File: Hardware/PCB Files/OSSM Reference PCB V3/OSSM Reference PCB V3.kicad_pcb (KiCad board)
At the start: 4 copper layers, 30 x 100 mm, 64 parts, among them J1 Screw_Terminal_01x02, J2 Screw_Terminal_01x02, J3 RJ45, J4 Conn_01x04, J5 USB_C_Receptacle_USB2.0_16P, J6 Conn_01x04, J7 Conn_01x03, Q1 BC817, Q2 BC817, Q4 40P04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

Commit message: Improved documentation and silkscreen
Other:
- board text added: "5V"
- board text added: "A"
- board text added: "B"
- board text added: "DIR"
- board text added: "GND"
- board text added: "IF YOU CAN READ THIS, YOU'VE VOIDED THE WARRANTY"
- board text added: "MTR+"
- board text added: "OSSM v3.0 Beta 1 2024/08/21"
- board text added: "PUL"
- board text added: "VDD"
- board text added: "VOID MY WARRANTY BABY! THIS IS OPEN SOURCE!!!"

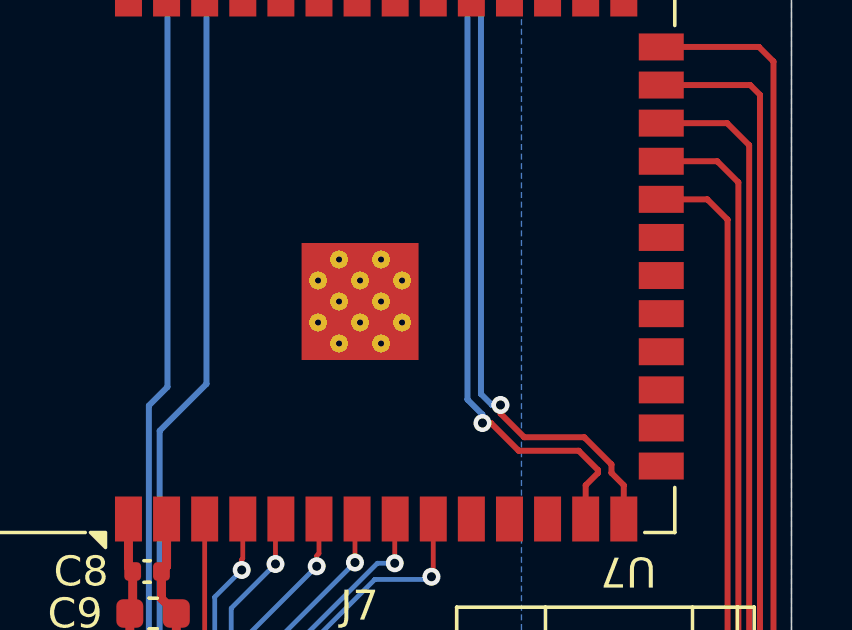
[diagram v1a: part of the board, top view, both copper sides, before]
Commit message: Last double check before ordering
Add Test points and Resistor Part numbers
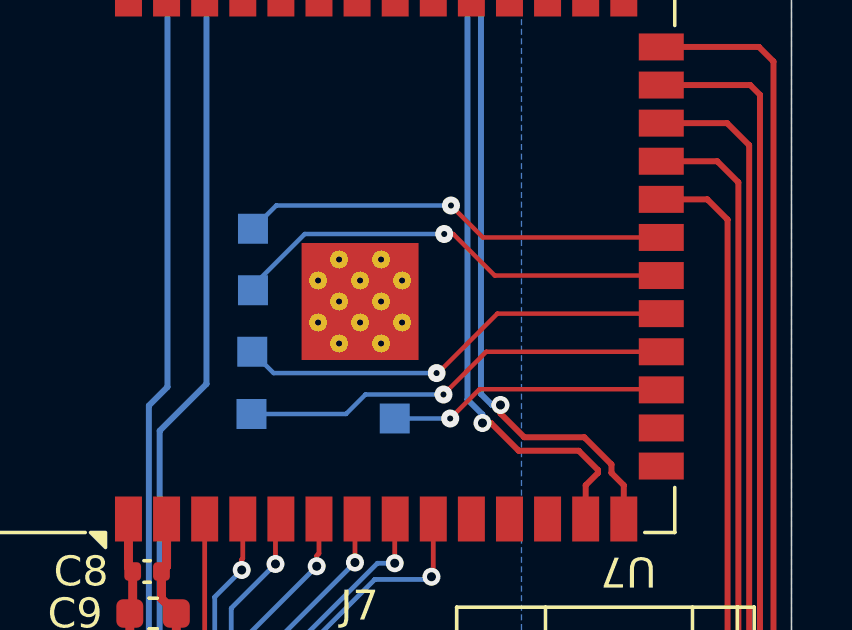
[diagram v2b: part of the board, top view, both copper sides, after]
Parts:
- added TP1: TestPoint, TestPoint:TestPoint_Pad_1.0x1.0mm, B.Cu at (81.8, 89.2)
- added TP2: TestPoint, TestPoint:TestPoint_Pad_1.0x1.0mm, B.Cu at (77.0, 89.0)
- added TP3: TestPoint, TestPoint:TestPoint_Pad_1.0x1.0mm, B.Cu at (77.0, 86.9)
- added TP4: TestPoint, TestPoint:TestPoint_Pad_1.0x1.0mm, B.Cu at (77.0, 84.9)
- added TP5: TestPoint, TestPoint:TestPoint_Pad_1.0x1.0mm, B.Cu at (77.0, 82.8)
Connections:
- U7 pad 17: unconnected-(U7-IO9-Pad17) -> Net-(U7-IO9)
- U7 pad 18: unconnected-(U7-IO10-Pad18) -> Net-(U7-IO10)
- U7 pad 19: unconnected-(U7-IO11-Pad19) -> Net-(U7-IO11)
- U7 pad 20: unconnected-(U7-IO12-Pad20) -> Net-(U7-IO12)
- U7 pad 21: unconnected-(U7-IO13-Pad21) -> Net-(U7-IO13)
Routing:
- net Net-(U7-IO12): track 0.00 -> 15.0 mm, vias 0 -> 1
- net Net-(U7-IO11): track 0.00 -> 14.8 mm, vias 0 -> 1
- net Net-(U7-IO10): track 0.00 -> 14.5 mm, vias 0 -> 1
- net Net-(U7-IO13): track 0.00 -> 14.4 mm, vias 0 -> 1
- net Net-(U7-IO9): track 0.00 -> 9.30 mm, vias 0 -> 1
